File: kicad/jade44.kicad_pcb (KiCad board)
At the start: 2 copper layers, 148.7 x 111.8 mm, 56 parts

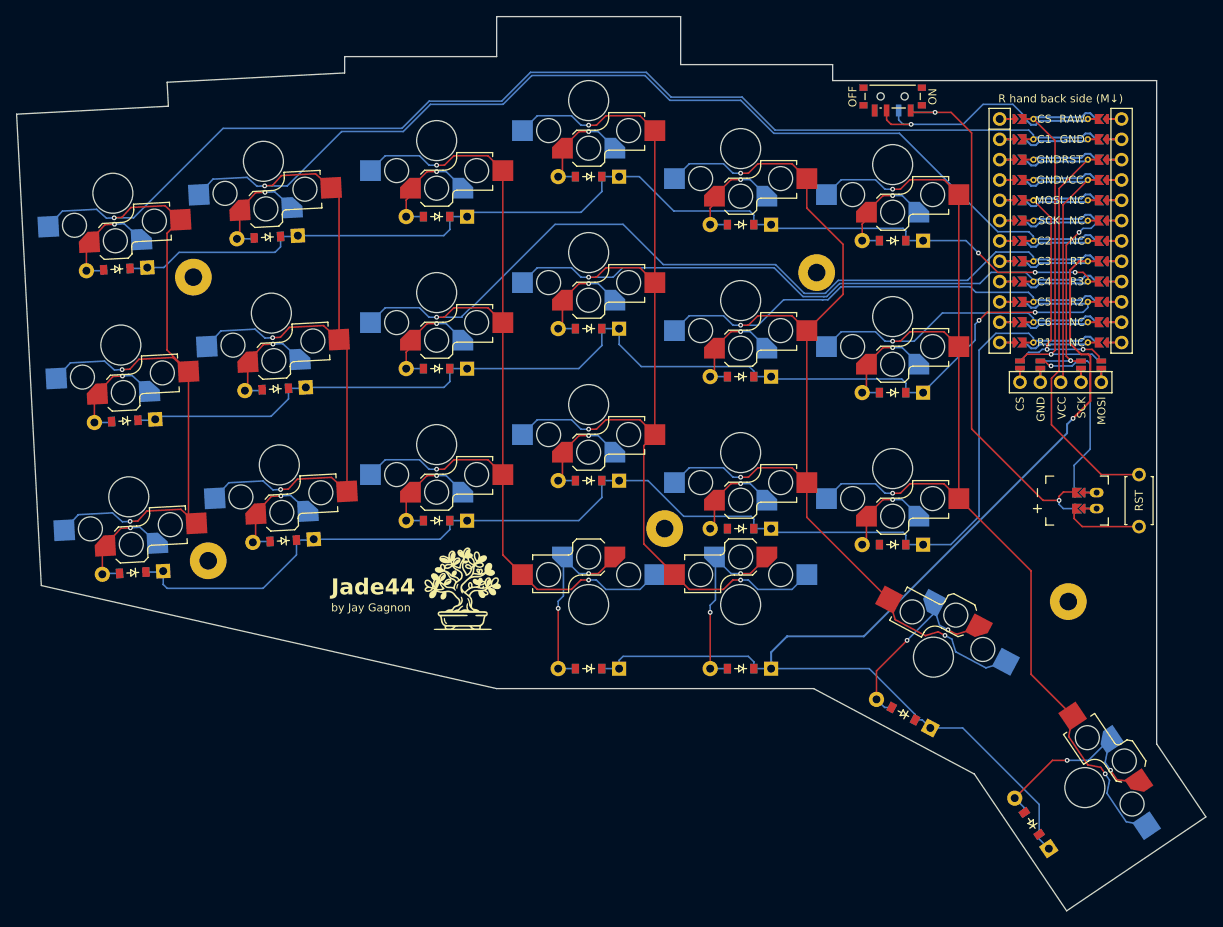
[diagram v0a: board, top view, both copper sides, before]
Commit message: Fillet pcb outline.
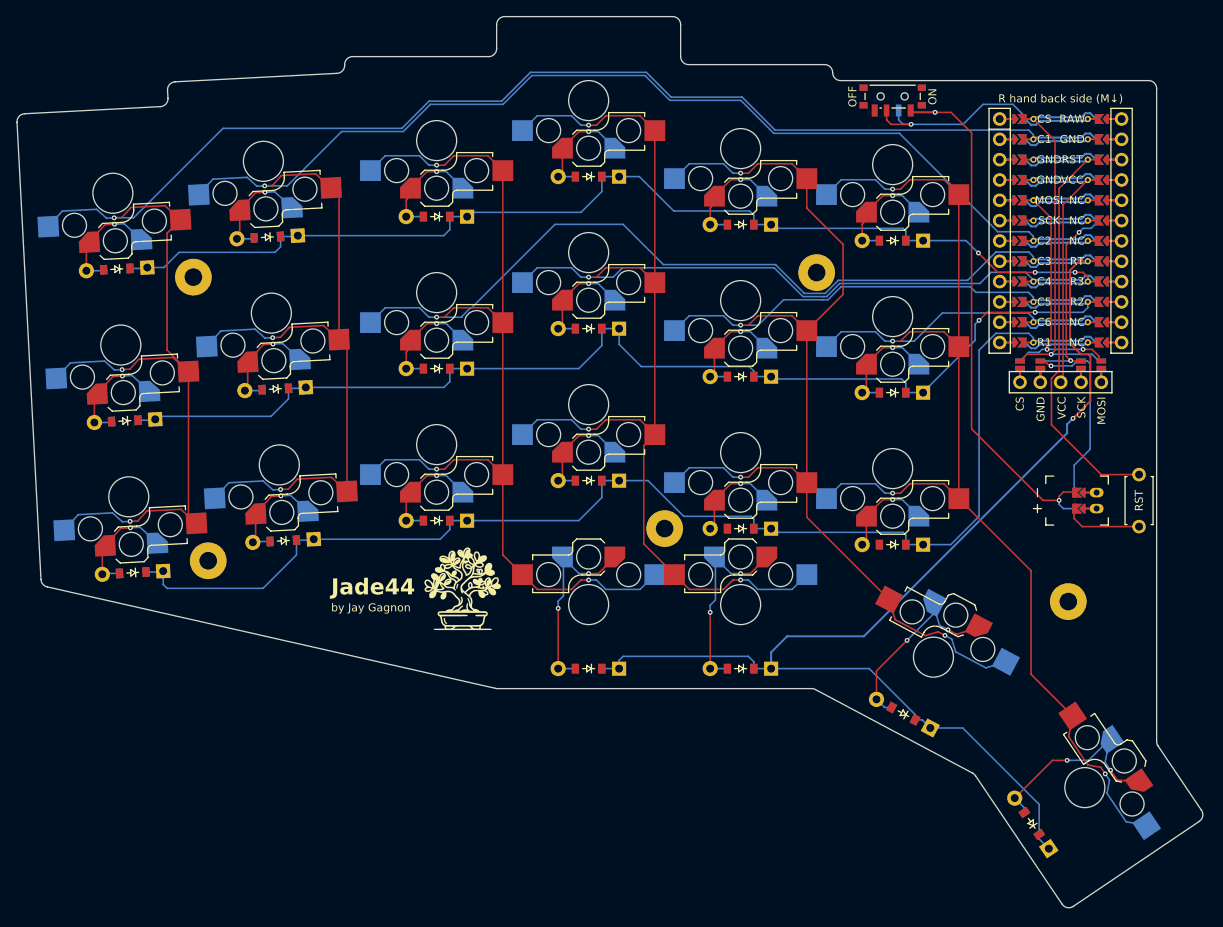
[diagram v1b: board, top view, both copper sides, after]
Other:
- board size 148.7 x 111.8 mm -> 148.2 x 111.4 mm
- rule pad_to_mask_clearance: 0.05 -> 0

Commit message: Address a pile of DRC issues.
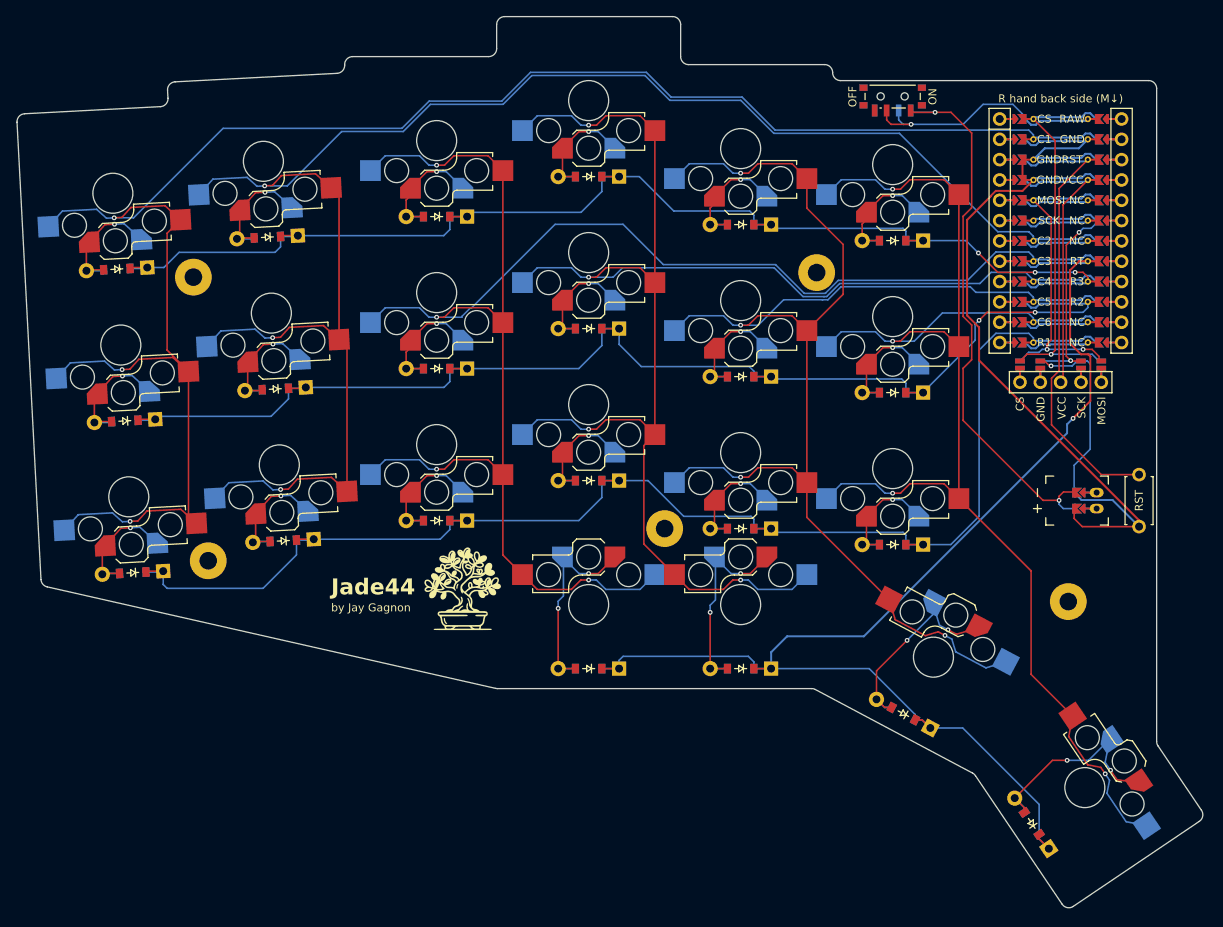
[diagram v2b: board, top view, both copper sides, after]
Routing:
- net GND: track 63.3 -> 141.2 mm
- net R3: track 144.3 -> 157.3 mm
- net R2: track 148.1 -> 161.2 mm
- net R1: track 159.9 -> 172.9 mm
- net RT: track 156.5 -> 165.5 mm
- net C6_R1: track 12.0 -> 16.4 mm
- net C5_R1: track 12.0 -> 16.4 mm
- net C5_RT: track 25.6 -> 27.9 mm
- net C6_RT: track 25.5 -> 27.8 mm
- net C1_R3: track 14.2 -> 16.4 mm
- net C2_R1: track 14.2 -> 16.4 mm
- net C1_R1: track 14.2 -> 16.4 mm
- net C1_R2: track 14.2 -> 16.4 mm
- net C2_R3: track 14.2 -> 16.4 mm
- net C2_R2: track 14.2 -> 16.4 mm
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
